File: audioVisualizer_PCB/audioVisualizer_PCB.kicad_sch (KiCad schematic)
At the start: 38 parts, among them J1 USB_C_16P, J2 SWD_DEBUG, J3 SPI_LED_MATRIX, U1 AMS1117-3.3, U7 STM32F401CCUx, Y1 ASE-25MHz

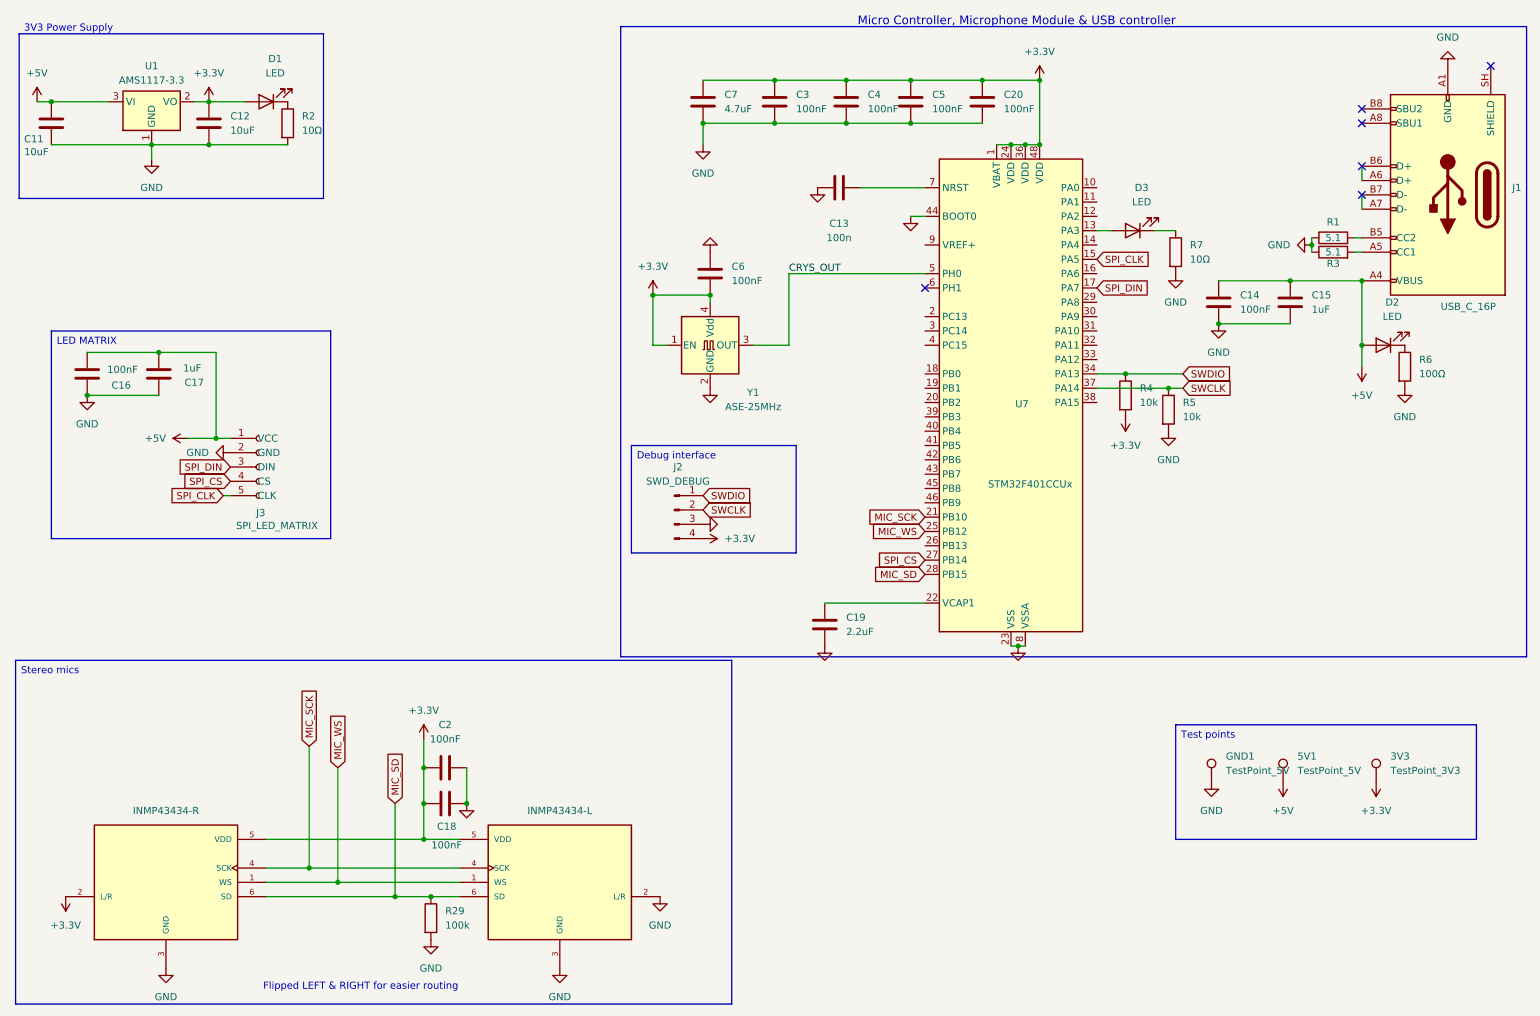
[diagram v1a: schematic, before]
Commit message: added cap for vref pin
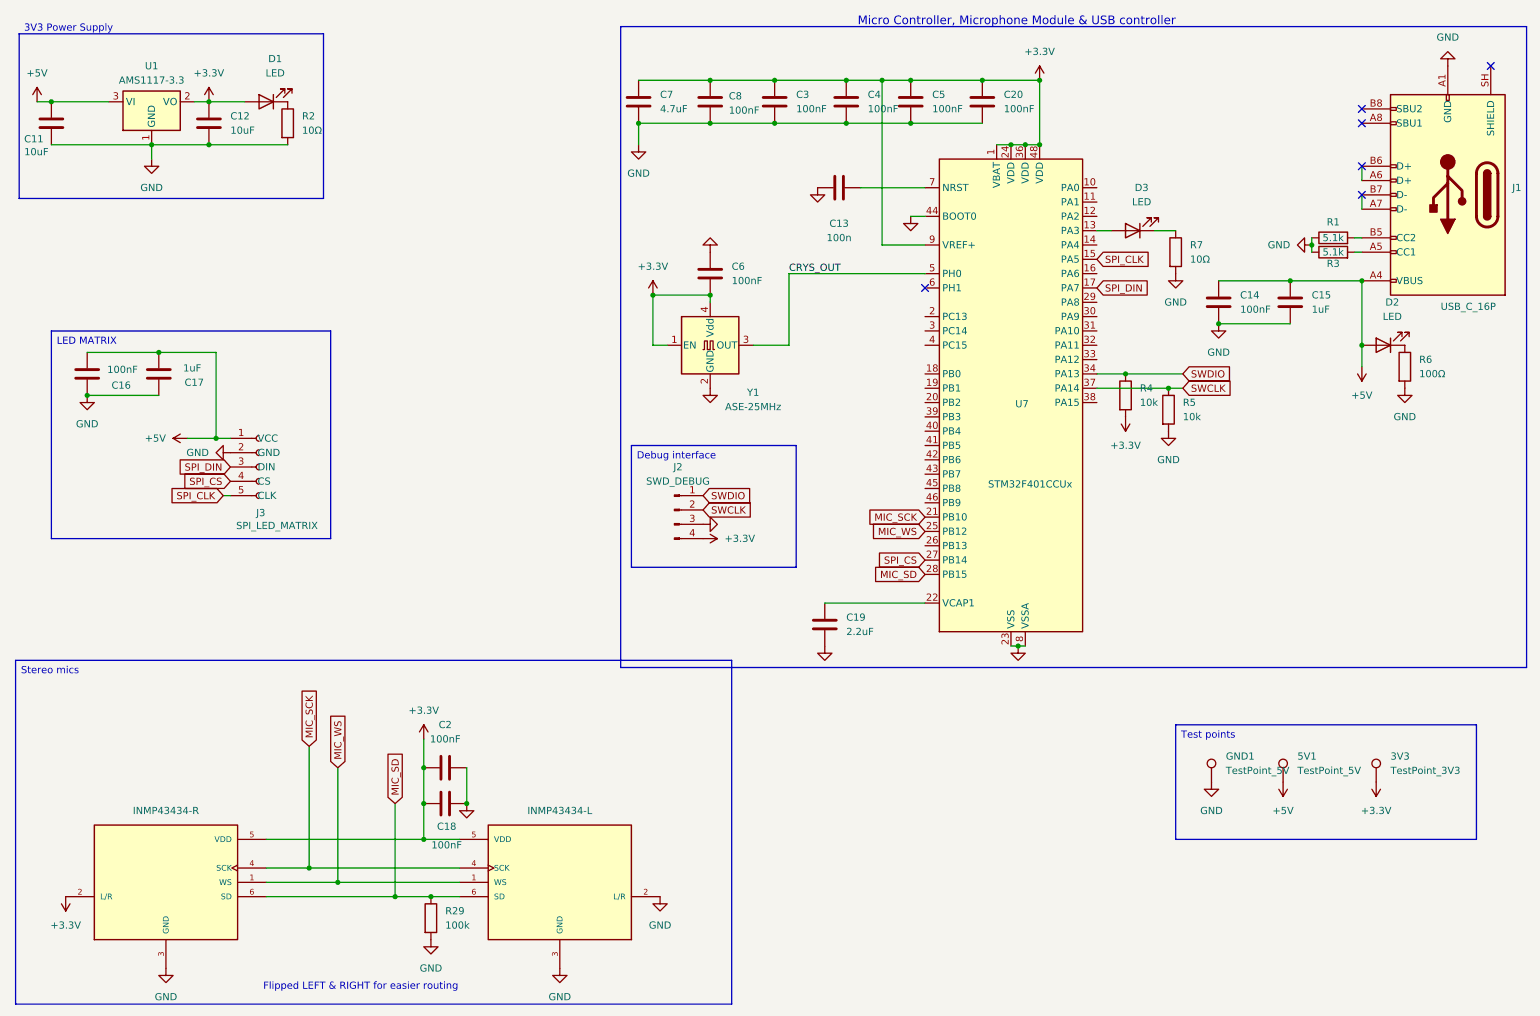
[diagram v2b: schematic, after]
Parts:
- added C8: 100nF, Capacitor_SMD:C_0805_2012Metric, symbol Device:C
- R1, R3: value 5.1 -> 5.1k
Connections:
- net +3.3V: now also U7.9 (VREF+), C8.1
- net GND: now also C8.2
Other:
- moved on the sheet: C7
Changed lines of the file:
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@@
 	(rectangle
 		(start 122.555 14.605)
-		(end 283.21 126.365)
+		(end 283.21 128.27)
 		(stroke
 			(width 0)
@@
 		(exclude_from_sim no)
 		(at 124.46 88.9 0)
-		(size 29.21 19.05)
+		(size 29.21 21.59)
 		(margins 0.9525 0.9525 0.9525 0.9525)
 		(stroke
@@
 	)
 	(junction
+		(at 168.91 24.13)
+		(diameter 0)
+		(color 0 0 0 0)
+	)
+	(junction
+		(at 138.43 24.13)
+		(diameter 0)
+		(color 0 0 0 0)
+	)
+	(junction
 		(at 241.3 59.69)
 		(diameter 0)
@@
 	)
 	(junction
-		(at 137.16 31.75)
-		(diameter 0)
-		(color 0 0 0 0)
-	)
-	(junction
 		(at 228.6 67.31)
 		(diameter 0)
@@
 	)
 	(junction
-		(at 149.86 24.13)
+		(at 125.73 31.75)
 		(diameter 0)
 		(color 0 0 0 0)
@@
 	)
 	(junction
+		(at 149.86 24.13)
+		(diameter 0)
+		(color 0 0 0 0)
+	)
+	(junction
 		(at 254 71.12)
 		(diameter 0)
@@
 	)
 	(junction
-		(at 149.86 31.75)
+		(at 194.31 35.56)
 		(diameter 0)
 		(color 0 0 0 0)
 	)
 	(junction
-		(at 194.31 35.56)
+		(at 149.86 31.75)
 		(diameter 0)
 		(color 0 0 0 0)
@@
 	)
 	(junction
+		(at 138.43 31.75)
+		(diameter 0)
+		(color 0 0 0 0)
+	)
+	(junction
 		(at 87.63 158.75)
 		(diameter 0)
@@
 	(wire
 		(pts
-			(xy 149.86 31.75) (xy 162.56 31.75)
+			(xy 222.25 76.2) (xy 212.09 76.2)
 		)
 		(stroke
@@
 	(wire
 		(pts
-			(xy 222.25 76.2) (xy 212.09 76.2)
+			(xy 152.4 58.42) (xy 176.53 58.42)
 		)
 		(stroke
@@
 	(wire
 		(pts
-			(xy 152.4 58.42) (xy 176.53 58.42)
+			(xy 173.99 24.13) (xy 186.69 24.13)
 		)
 		(stroke
@@
 	(wire
 		(pts
-			(xy 173.99 24.13) (xy 186.69 24.13)
+			(xy 72.39 166.37) (xy 93.98 166.37)
 		)
 		(stroke
@@
 	(wire
 		(pts
-			(xy 149.86 24.13) (xy 162.56 24.13)
+			(xy 191.77 35.56) (xy 194.31 35.56)
 		)
 		(stroke
@@
 	(wire
 		(pts
-			(xy 72.39 166.37) (xy 93.98 166.37)
+			(xy 128.27 71.12) (xy 130.81 71.12)
 		)
 		(stroke
@@
 	(wire
 		(pts
-			(xy 191.77 35.56) (xy 194.31 35.56)
+			(xy 63.5 35.56) (xy 49.53 35.56)
 		)
 		(stroke
@@
 	(wire
 		(pts
-			(xy 128.27 71.12) (xy 130.81 71.12)
+			(xy 252.73 52.07) (xy 254 52.07)
 		)
 		(stroke
@@
 	(wire
 		(pts
-			(xy 63.5 35.56) (xy 49.53 35.56)
+			(xy 176.53 53.34) (xy 168.91 53.34)
 		)
 		(stroke
@@
 	(wire
 		(pts
-			(xy 252.73 52.07) (xy 254 52.07)
+			(xy 88.9 168.91) (xy 93.98 168.91)
 		)
 		(stroke
@@
 	(wire
 		(pts
-			(xy 88.9 168.91) (xy 93.98 168.91)
+			(xy 149.86 24.13) (xy 162.56 24.13)
 		)
 		(stroke
@@
 	(wire
 		(pts
-			(xy 137.16 24.13) (xy 149.86 24.13)
+			(xy 125.73 24.13) (xy 138.43 24.13)
 		)
 		(stroke
@@
 	(wire
 		(pts
-			(xy 137.16 31.75) (xy 137.16 35.56)
+			(xy 125.73 31.75) (xy 138.43 31.75)
+		)
+		(stroke
+			(width 0)
+			(type default)
+		)
+	)
+	(wire
+		(pts
+			(xy 125.73 31.75) (xy 125.73 35.56)
 		)
 		(stroke
@@
 	(wire
 		(pts
+			(xy 138.43 31.75) (xy 149.86 31.75)
+		)
+		(stroke
+			(width 0)
+			(type default)
+		)
+	)
+	(wire
+		(pts
 			(xy 39.37 38.1) (xy 39.37 35.56)
 		)
@@
 	(wire
 		(pts
+			(xy 168.91 53.34) (xy 168.91 24.13)
+		)
+		(stroke
+			(width 0)
+			(type default)
+		)
+	)
+	(wire
+		(pts
+			(xy 149.86 31.75) (xy 162.56 31.75)
+		)
+		(stroke
+			(width 0)
+			(type default)
+		)
+	)
+	(wire
+		(pts
 			(xy 59.69 166.37) (xy 72.39 166.37)
 		)
@@
 	(wire
 		(pts
-			(xy 162.56 24.13) (xy 173.99 24.13)
+			(xy 162.56 24.13) (xy 168.91 24.13)
 		)
 		(stroke
@@
 	(wire
 		(pts
+			(xy 168.91 24.13) (xy 173.99 24.13)
+		)
+		(stroke
+			(width 0)
+			(type default)
+		)
+	)
+	(wire
+		(pts
 			(xy 241.3 59.69) (xy 254 59.69)
 		)
@@
 	(wire
 		(pts
-			(xy 137.16 31.75) (xy 149.86 31.75)
+			(xy 82.55 168.91) (xy 82.55 152.4)
 		)
 		(stroke
@@
 	(wire
 		(pts
-			(xy 82.55 168.91) (xy 82.55 152.4)
+			(xy 49.53 27.94) (xy 55.88 27.94)
 		)
 		(stroke
@@
 	(wire
 		(pts
-			(xy 49.53 27.94) (xy 55.88 27.94)
+			(xy 87.63 158.75) (xy 87.63 152.4)
 		)
 		(stroke
@@
 	(wire
 		(pts
-			(xy 87.63 158.75) (xy 87.63 152.4)
+			(xy 186.69 24.13) (xy 196.85 24.13)
 		)
 		(stroke
@@
 	(wire
 		(pts
-			(xy 186.69 24.13) (xy 196.85 24.13)
+			(xy 138.43 24.13) (xy 149.86 24.13)
 		)
 		(stroke
@@
 	(symbol
 		(lib_id "Device:C")
-		(at 137.16 27.94 0)
+		(at 125.73 27.94 0)
 		(unit 1)
 		(body_style 1)
@@
 		(dnp no)
 		(property "Reference" "C7"
-			(at 140.97 26.6699 0)
+			(at 129.54 26.6699 0)
 			(show_name no)
 			(do_not_autoplace no)
@@
 		)
 		(property "Value" "4.7uF"
-			(at 140.97 29.21 0)
+			(at 129.54 29.21 0)
 			(show_name no)
 			(do_not_autoplace no)
@@
 		)
 		(property "Footprint" "Capacitor_SMD:C_0805_2012Metric"
-			(at 138.1252 31.75 0)
+			(at 126.6952 31.75 0)
 			(hide yes)
 			(show_name no)
@@
 		)
 		(property "Datasheet" ""
-			(at 137.16 27.94 0)
+			(at 125.73 27.94 0)
 			(hide yes)
 			(show_name no)
@@
 		)
 		(property "Description" "Unpolarized capacitor"
-			(at 137.16 27.94 0)
+			(at 125.73 27.94 0)
 			(hide yes)
 			(show_name no)
@@
 			)
 		)
-		(property "Value" "5.1"
+		(property "Value" "5.1k"
 			(at 248.92 52.07 90)
 			(show_name no)
@@
 			)
 		)
-		(property "Value" "5.1"
+		(property "Value" "5.1k"
 			(at 248.92 54.61 90)
 			(show_name no)
@@
 	(symbol
 		(lib_id "power:GND")
-		(at 137.16 35.56 0)
+		(at 125.73 35.56 0)
 		(unit 1)
 		(body_style 1)
@@
 		(fields_autoplaced yes)
 		(property "Reference" "#PWR05"
-			(at 137.16 41.91 0)
+			(at 125.73 41.91 0)
 			(hide yes)
 			(show_name no)
@@
 		)
 		(property "Value" "GND"
-			(at 137.16 40.64 0)
+			(at 125.73 40.64 0)
 			(show_name no)
 			(do_not_autoplace no)
@@
 		)
 		(property "Footprint" ""
-			(at 137.16 35.56 0)
+			(at 125.73 35.56 0)
 			(hide yes)
 			(show_name no)
@@
 		)
 		(property "Datasheet" ""
-			(at 137.16 35.56 0)
+			(at 125.73 35.56 0)
 			(hide yes)
 			(show_name no)
@@
 		)
 		(property "Description" "Power symbol creates a global label with name \"GND\" , ground"
-			(at 137.16 35.56 0)
+			(at 125.73 35.56 0)
 			(hide yes)
 			(show_name no)
@@
 					(unit 1)
 				)
+			)
+		)
+	)
+	(symbol
+		(lib_id "Device:C")
+		(at 138.43 27.94 0)
+		(unit 1)
+		(body_style 1)
+		(exclude_from_sim no)
+		(in_bom yes)
+		(on_board yes)
+		(in_pos_files yes)
+		(dnp no)
+		(property "Reference" "C8"
+			(at 141.732 26.924 0)
+			(show_name no)
+			(do_not_autoplace no)
+			(effects
+				(font
+					(size 1.27 1.27)
+				)
+				(justify left)
+			)
+		)
+		(property "Value" "100nF"
+			(at 141.732 29.464 0)
+			(show_name no)
+			(do_not_autoplace no)
+			(effects
+				(font
+					(size 1.27 1.27)
+				)
+				(justify left)
+			)
+		)
+		(property "Footprint" "Capacitor_SMD:C_0805_2012Metric"
+			(at 139.3952 31.75 0)
+			(hide yes)
+			(show_name no)
+			(do_not_autoplace no)
+			(effects
+				(font
+					(size 1.27 1.27)
+				)
+			)
+		)
+		(property "Datasheet" ""
+			(at 138.43 27.94 0)
+			(hide yes)
+			(show_name no)
+			(do_not_autoplace no)
+			(effects
+				(font
+					(size 1.27 1.27)
+				)
+			)
+		)
+		(property "Description" "Unpolarized capacitor"
+			(at 138.43 27.94 0)
+			(hide yes)
+			(show_name no)
+			(do_not_autoplace no)
+			(effects
+				(font
+					(size 1.27 1.27)
+				)
+			)
+		)
+		(pin "1"
+		)
+		(pin "2"
+		)
+		(instances
+			(project "audioVisualizer_PCB"
+				(path "/8779f4c0-fa76-4e9c-9285-12099bba0fb4"
+					(reference "C8")
+					(unit 1)
+				)
